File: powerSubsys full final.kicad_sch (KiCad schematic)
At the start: 74 parts, among them J1 Conn_02x16_Odd_Even, J2 JST_PH_2mm, Q2 S9013 J3(RANGE:200-350), SW1 SS-12D11G3R, U1 INA219AIDR, U10 TPS63020DSJR, U2 DRV8833PWR, U3 BQ24074RGT, U4 TPS22810DRVR, U5 TPS22810DRVR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

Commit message: Added power flags
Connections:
- no-connect marks 22 -> 24

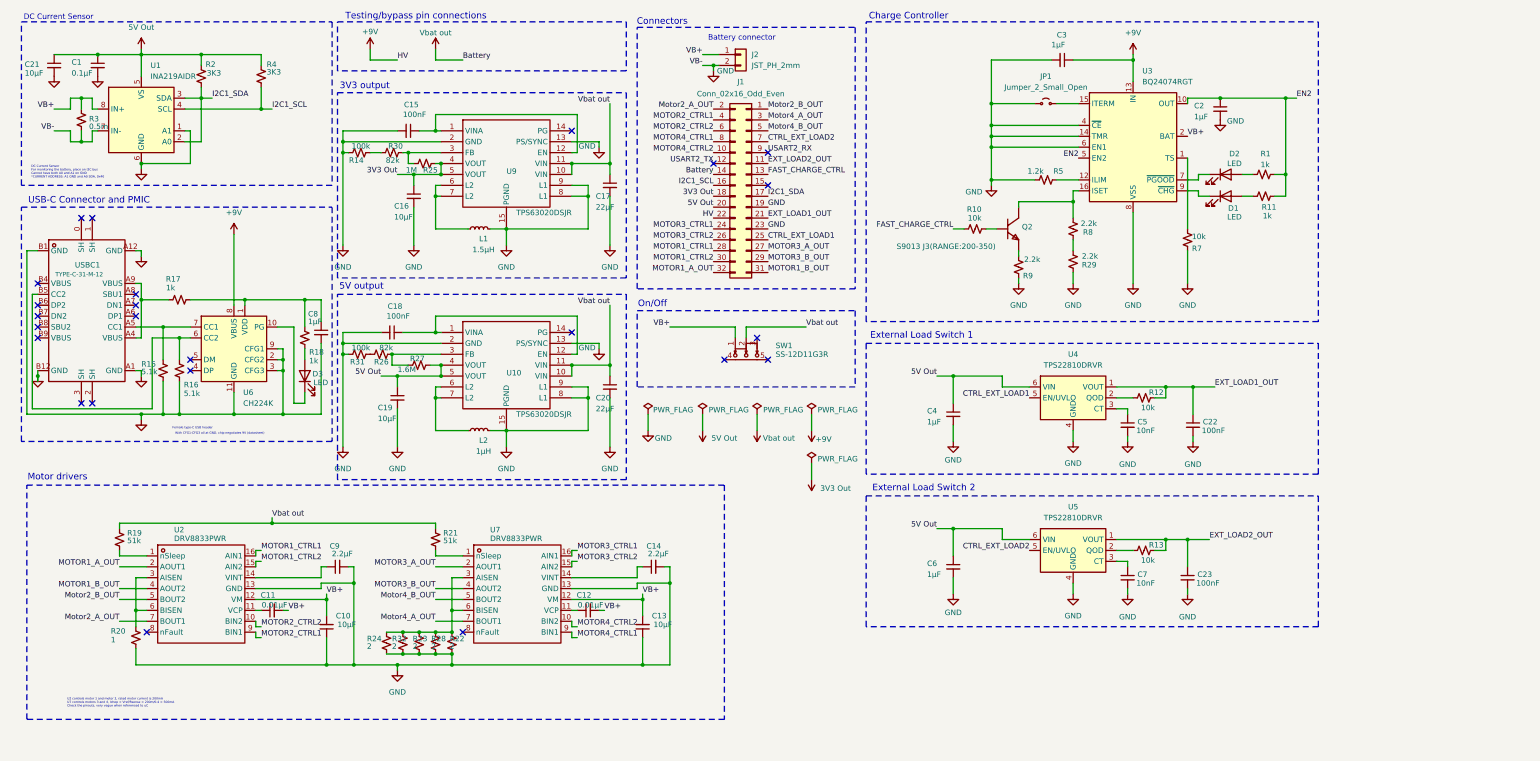
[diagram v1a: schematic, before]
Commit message: Added voltage regulator
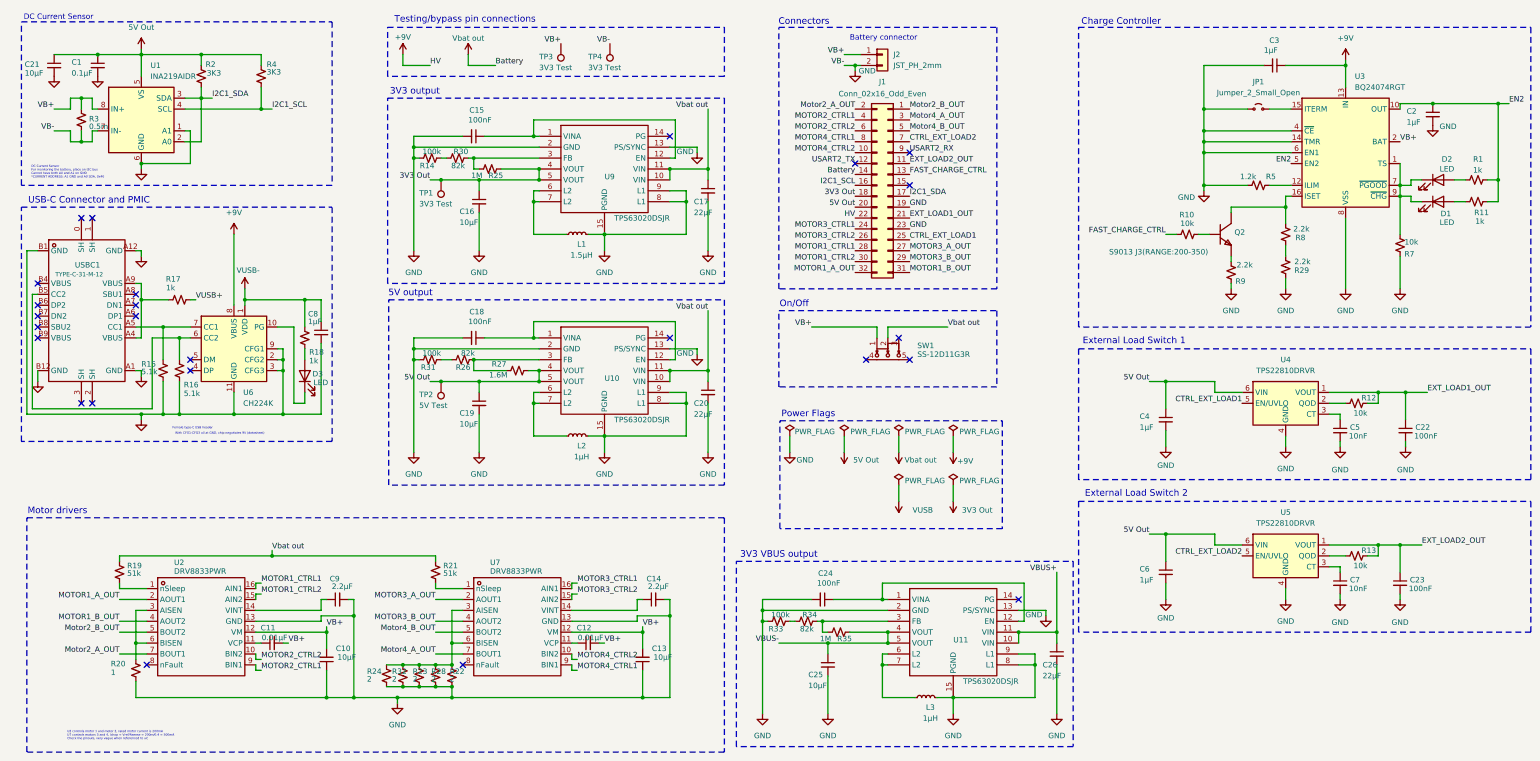
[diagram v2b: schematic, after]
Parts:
- added C24: 100nF, Library:C0603, symbol Device:C_Small
- added C25: 10μF, Library:C0805, symbol Device:C_Small
- added C26: 22μF, Library:C1206, symbol Device:C_Small
- added L3: 1μH, Library:L1008, symbol Device:L_Small
- added R33: 100k, Library:C1206, symbol Device:R_Small_US
- added R34: 82k, Library:C0603, symbol Device:R_Small_US
- added R35: 1M, Library:C1206, symbol Device:R_Small_US
- added TP1, TP3, TP4: 3V3 Test, symbol Connector:TestPoint
- added TP2: 5V Test, symbol Connector:TestPoint
- added U11: TPS63020DSJR, Library:VSON-14_L4.0-W3.0-P0.50-BL-EP_TI_DSJ, symbol TPS63020DSJR1_TPS63020DSJR-altium-import:root_0_TPS63020DSJR_
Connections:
- net 3V3 Out: now also TP1.1
- net 5V Out: now also TP2.1
- net GND: now also C24.2, C25.2, C26.2, L3.2, R33.1, TP4.1, U11.13 (PS/SYNC), U11.15 (PGND), U11.2 (GND), U11.8 (L1), U11.9 (L1)
- net VB+: now also TP3.1
- net VUSB-: now reaches C8.1, R18.1, U6.1 (VDD)
- net VUSB-: no longer R17.2
- net at D2.1 (K), U3.7 (~{PGOOD}): now also D1.1 (K), R7.1, U3.1 (TS), U3.9 (~{CHG})
- new net: R33.2, R34.1
- new net: R34.2, R35.1, U11.3 (FB)
- new net: L3.1, U11.6 (L2), U11.7 (L2)
- new net: C24.1, U11.1 (VINA), U11.12 (EN)
- new net VBUS+: C26.1, U11.10 (VIN), U11.11 (VIN)
- new net VBUS-: C25.1, R35.2, U11.4 (VOUT), U11.5 (VOUT)
- new net VUSB+: R17.2
- no-connect marks 24 -> 25
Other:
- note added: "3V3 VBUS output"
- note added: "Power Flags"
- moved on the sheet: C10, C11, C12, C13, C14, C15, C16, C17, C18, C19, C2, C20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

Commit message: Final
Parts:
- removed L3: 1μH, Library:L1008, symbol Device:L_Small
- removed R17: 1k, Library:C0603, symbol Device:R_Small_US
- removed R34: 82k, Library:C0603, symbol Device:R_Small_US
- removed R35: 1M, Library:C1206, symbol Device:R_Small_US
- removed U11: TPS63020DSJR, Library:VSON-14_L4.0-W3.0-P0.50-BL-EP_TI_DSJ, symbol TPS63020DSJR1_TPS63020DSJR-altium-import:root_0_TPS63020DSJR_
- added TP5: TP +9V, TestPoint:TestPoint_Pad_D1.5mm, symbol Connector:TestPoint
- added TP6: TP VBUS, TestPoint:TestPoint_Pad_D1.5mm, symbol Connector:TestPoint
- added TP7: TS Vsupply, TestPoint:TestPoint_Pad_D1.5mm, symbol Connector:TestPoint
- added TP8: TP VREG, TestPoint:TestPoint_Pad_D1.5mm, symbol Connector:TestPoint
- added U8: L78L33ACUTR, Package_TO_SOT_SMD:SOT-89-3, symbol Regulator_Linear:L78L33_SOT89
- C24: value 100nF -> 1μF; footprint Library:C0603 -> Library:C0805
- C25: value 10μF -> 100nF
- C26: value 22μF -> 10μF; footprint Library:C1206 -> Library:C0805
- D1, D2, D3: value LED -> KT-0805G
- J2: footprint Connector_JST:JST_PH_S2B-PH-SM4-TB_1x02-1MP_P2.00mm_Horizontal -> Connector_JST:JST_PH_S2B-PH-K_1x02_P2.00mm_Horizontal
- JP1: value Jumper_2_Small_Open -> JP RITERM
- R33: value 100k -> 10k; footprint Library:C1206 -> Library:C0603
- TP1: value 3V3 Test -> TP 3V3; footprint (none) -> TestPoint:TestPoint_Pad_D1.5mm
- TP2: value 5V Test -> TP 5V; footprint (none) -> TestPoint:TestPoint_Pad_D1.5mm
- TP3: value 3V3 Test -> TP VBat+; footprint (none) -> TestPoint:TestPoint_Pad_D1.5mm
- TP4: value 3V3 Test -> TP GND; footprint (none) -> TestPoint:TestPoint_Pad_D1.5mm
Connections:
- net VBUS+ is gone; now on net Battery: C26.1
- net VBUS- is gone; now on net GND: C25.1
- net +9V: now also C24.2, R33.1, USBC1.A4 (VBUS), USBC1.A9 (VBUS), TP5.1, TP6.1, U8.3 (IN); no longer U6.8 (VBUS)
- net GND: now also C24.1, U8.2 (GND); no longer C24.2, C25.2, R33.1
- net Motor4_A_OUT: now also R22.1, R23.1, R24.1, R28.1, R32.1, U7.3 (AISEN), U7.6 (BISEN)
- net at R33.2: now also U6.8 (VBUS)
- net DP: now reaches U6.4 (DP)
- net DP: now also USBC1.A6 (DP1)
- net DM: now reaches U6.5 (DM)
- net DM: now also USBC1.A7 (DN1)
- net VB+ renamed Battery
- net Battery: now also J1.14 (Pin_14); no longer C10.2, C11.2, C12.2, C13.2, U2.12 (VM), U7.12 (VM)
- net VUSB- renamed VREG
- net VREG: now also C25.2, TP8.1, U8.1 (OUT)
- net Vbat out renamed Vsupply
- net Vsupply: now also C10.2, C11.2, C12.2, C13.2, U2.12 (VM), U7.12 (VM), TP7.1; no longer J1.14 (Pin_14)
- new net: D2.1 (K), U3.7 (~{PGOOD})
- new net: D1.1 (K), U3.9 (~{CHG})
- new net: R7.1, U3.1 (TS)
- no-connect marks 25 -> 20
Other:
- note added: "3V3 VBUS LDO"
- note removed: "3V3 VBUS output"
- moved on the sheet: C8, D3, R16, R18, R20, R22, R23, R24, R28, R32, TP3

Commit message: Add files via upload
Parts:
- removed JP1: JP RITERM, Library:C1206, symbol Jumper:Jumper_2_Small_Open
- added JP2: SolderJumper_2_Open, Jumper:SolderJumper-2_P1.3mm_Open_RoundedPad1.0x1.5mm, symbol Jumper:SolderJumper_2_Open
- C1: value 0.1μF -> 100nF
- C10, C13, C16, C19, C21, C26: value 10μF -> 10uF
- C11, C12: value 0.01μF -> 10nF
- C14, C9: value 2.2μF -> 2.2uF
- C17, C20: value 22μF -> 22uF
- C2, C24, C3, C4, C6, C8: value 1μF -> 1uF
- C25: footprint Library:C0805 -> Library:C0603
- J1, J2: now not fitted; now left out of the parts list
- L1: value 1.5μH -> 1.5uH
- L2: value 1μH -> 1uH
- Q2: LCSC (none) -> C6749
- R33: footprint Library:C0603 -> Library:C0805
- TP1, TP2, TP3, TP4, TP5, TP6, TP7, TP8: now left out of the parts list
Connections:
- net GND: now also JP2.1 (A)
- net Motor4_A_OUT: no longer R22.1, R23.1, R24.1, R28.1, R32.1, U7.3 (AISEN), U7.6 (BISEN)
- net at U3.15 (ITERM): now also JP2.2 (B)
- new net: R22.1, R23.1, R24.1, R28.1, R32.1, U7.3 (AISEN), U7.6 (BISEN)
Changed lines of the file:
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@@
 	)
 	(junction
-		(at 114.3 162.56)
-		(diameter 0)
-		(color 0 0 0 0)
-	)
-	(junction
 		(at 69.85 35.56)
 		(diameter 0)
@@
 	(wire
 		(pts
-			(xy 114.3 162.56) (xy 114.3 160.02)
-		)
-		(stroke
-			(width 0)
-			(type default)
-		)
-	)
-	(wire
-		(pts
 			(xy 231.14 111.76) (xy 231.14 115.57)
 		)
@@
 	(wire
 		(pts
-			(xy 289.56 35.56) (xy 299.72 35.56)
+			(xy 289.56 35.56) (xy 298.45 35.56)
 		)
 		(stroke
@@
 	(wire
 		(pts
-			(xy 110.49 162.56) (xy 114.3 162.56)
+			(xy 110.49 162.56) (xy 116.84 162.56)
 		)
 		(stroke
@@
 	(wire
 		(pts
-			(xy 304.8 35.56) (xy 309.88 35.56)
+			(xy 322.58 25.4) (xy 322.58 30.48)
 		)
 		(stroke
@@
 	(wire
 		(pts
-			(xy 322.58 25.4) (xy 322.58 30.48)
+			(xy 306.07 35.56) (xy 309.88 35.56)
 		)
 		(stroke
@@
 	(wire
 		(pts
-			(xy 114.3 162.56) (xy 116.84 162.56)
-		)
-		(stroke
-			(width 0)
-			(type default)
-		)
-	)
-	(wire
-		(pts
 			(xy 142.24 154.94) (xy 157.48 154.94)
 		)
@@
 	(wire
 		(pts
-			(xy 114.3 162.56) (xy 114.3 167.64)
+			(xy 114.3 160.02) (xy 114.3 167.64)
 		)
 		(stroke
@@
 			)
 		)
-		(property "Value" "2.2μF"
+		(property "Value" "2.2uF"
 			(at 91.186 146.812 90)
 			(effects
@@
 			)
 		)
-		(property "Value" "10μF"
+		(property "Value" "10uF"
 			(at 91.948 163.322 0)
 			(effects
@@
 			)
 		)
-		(property "Value" "1μH"
+		(property "Value" "1uH"
 			(at 144.526 116.586 90)
 			(effects
@@
 			)
 		)
-		(property "Value" "1μF"
+		(property "Value" "1uF"
 			(at 303.53 21.844 90)
 			(effects
@@
 			)
 		)
-		(property "Footprint" "Library:C0603"
+		(property "Footprint" "Library:C0805"
 			(at 60.96 73.66 0)
 			(effects
@@
 			)
 		)
-		(property "Value" "10μF"
+		(property "Value" "10uF"
 			(at 165.608 163.322 0)
 			(effects
@@
 			)
 		)
-		(property "Value" "1μF"
+		(property "Value" "1uF"
 			(at 336.804 38.608 0)
 			(effects
@@
 		(unit 1)
 		(exclude_from_sim no)
-		(in_bom yes)
+		(in_bom no)
 		(on_board yes)
 		(dnp no)
@@
 			)
 		)
-		(property "Value" "0.01μF"
+		(property "Value" "10nF"
 			(at 75.946 158.75 90)
 			(effects
@@
 			)
 		)
-		(property "Value" "10μF"
+		(property "Value" "10uF"
 			(at 116.078 61.976 0)
 			(effects
@@
 	)
 	(symbol
-		(lib_id "Jumper:Jumper_2_Small_Open")
-		(at 302.26 35.56 0)
-		(unit 1)
-		(exclude_from_sim yes)
-		(in_bom yes)
-		(on_board yes)
-		(dnp no)
-		(fields_autoplaced yes)
-		(property "Reference" "JP1"
-			(at 302.26 29.21 0)
-			(effects
-				(font
-					(size 1.27 1.27)
-				)
-			)
-		)
-		(property "Value" "JP RITERM"
-			(at 302.26 31.75 0)
-			(effects
-				(font
-					(size 1.27 1.27)
-				)
-			)
-		)
-		(property "Footprint" "Library:C1206"
-			(at 302.26 35.56 0)
-			(effects
-				(font
-					(size 1.27 1.27)
-				)
-				(hide yes)
-			)
-		)
-		(property "Datasheet" "~"
-			(at 302.26 35.56 0)
-			(effects
-				(font
-					(size 1.27 1.27)
-				)
-				(hide yes)
-			)
-		)
-		(property "Description" "Jumper, 2-pole, small symbol, open"
-			(at 302.26 35.56 0)
-			(effects
-				(font
-					(size 1.27 1.27)
-				)
-				(hide yes)
-			)
-		)
-		(pin "1"
-		)
-		(pin "2"
-		)
-		(instances
-			(project "powerSubsys full"
-				(path "/7765ff1a-d3b4-4c36-a374-0b467da55076"
-					(reference "JP1")
-					(unit 1)
-				)
-			)
-		)
-	)
-	(symbol
 		(lib_id "power:GND")
 		(at 322.58 77.47 0)
@@
 			)
 		)
-		(property "Value" "1μF"
+		(property "Value" "1uF"
 			(at 210.058 163.322 0)
 			(effects
@@
 			)
 		)
-		(property "Value" "22μF"
+		(property "Value" "22uF"
 			(at 170.688 106.68 0)
 			(effects
@@
 			)
 		)
-		(property "Value" "22μF"
+		(property "Value" "22uF"
 			(at 170.688 59.69 0)
 			(effects
@@
 		(unit 1)
 		(exclude_from_sim no)
-		(in_bom yes)
+		(in_bom no)
 		(on_board yes)
 		(dnp no)
@@
 			)
 		)
-		(property "Value" "0.1μF"
+		(property "Value" "100nF"
 			(at 25.654 27.178 0)
 			(effects
@@
 			)
 		)
-		(property "Value" "0.01μF"
+		(property "Value" "10nF"
 			(at 149.606 158.75 90)
 			(effects
@@
 		(unit 1)
 		(exclude_from_sim no)
-		(in_bom yes)
+		(in_bom no)
 		(on_board yes)
-		(dnp no)
+		(dnp yes)
 		(fields_autoplaced yes)
 		(property "Reference" "J2"
@@
 			)
 		)
-		(property "Value" "1.5μH"
+		(property "Value" "1.5uH"
 			(at 144.526 69.596 90)
 			(effects
@@
 			)
 		)
-		(property "Value" "1μF"
+		(property "Value" "1uF"
 			(at 85.852 85.09 0)
 			(effects
@@
 			)
 		)
-		(property "Footprint" "Library:C0805"
+		(property "Footprint" "Library:C0603"
 			(at 231.14 163.83 0)
 			(effects
@@
 		(unit 1)
 		(exclude_from_sim no)
-		(in_bom yes)
+		(in_bom no)
 		(on_board yes)
 		(dnp no)
@@
 		(unit 1)
 		(exclude_from_sim no)
-		(in_bom yes)
+		(in_bom no)
 		(on_board yes)
-		(dnp no)
+		(dnp yes)
 		(property "Reference" "J1"
 			(at 214.63 29.21 0)
@@
 		(unit 1)
 		(exclude_from_sim no)
-		(in_bom yes)
+		(in_bom no)
 		(on_board yes)
 		(dnp no)
@@
 		(unit 1)
 		(exclude_from_sim no)
-		(in_bom yes)
+		(in_bom no)
 		(on_board yes)
 		(dnp no)
@@
 	)
 	(symbol
+		(lib_id "Jumper:SolderJumper_2_Open")
+		(at 302.26 35.56 0)
+		(unit 1)
+		(exclude_from_sim no)
+		(in_bom no)
+		(on_board yes)
+		(dnp no)
+		(fields_autoplaced yes)
+		(property "Reference" "JP2"
+			(at 302.26 29.21 0)
+			(effects
+				(font
+					(size 1.27 1.27)
+				)
+			)
+		)
+		(property "Value" "SolderJumper_2_Open"
+			(at 302.26 31.75 0)
+			(effects
+				(font
+					(size 1.27 1.27)
+				)
+			)
+		)
+		(property "Footprint" "Jumper:SolderJumper-2_P1.3mm_Open_RoundedPad1.0x1.5mm"
+			(at 302.26 35.56 0)
+			(effects
+				(font
+					(size 1.27 1.27)
+				)
+				(hide yes)
+			)
+		)
+		(property "Datasheet" "~"
+			(at 302.26 35.56 0)
+			(effects
+				(font
+					(size 1.27 1.27)
+				)
+				(hide yes)
+			)
+		)
+		(property "Description" "Solder Jumper, 2-pole, open"
+			(at 302.26 35.56 0)
+			(effects
+				(font
+					(size 1.27 1.27)
+				)
+				(hide yes)
+			)
+		)
+		(pin "2"
+		)
+		(pin "1"
+		)
+		(instances
+			(project ""
+				(path "/7765ff1a-d3b4-4c36-a374-0b467da55076"
+					(reference "JP2")
+					(unit 1)
+				)
+			)
+		)
+	)
+	(symbol
 		(lib_id "Device:C_Small")
 		(at 280.67 107.95 0)
@@
 			)
 		)
-		(property "Value" "1μF"
+		(property "Value" "1uF"
 			(at 274.574 109.728 0)
 			(effects
@@
 			)
 		)
-		(property "Value" "10μF"
+		(property "Value" "10uF"
 			(at 116.078 108.966 0)
 			(effects
@@
 			)
 		)
-		(property "Value" "1μF"
+		(property "Value" "1uF"
 			(at 274.574 145.288 0)
 			(effects
@@
 			)
 		)
-		(property "Value" "10μF"
+		(property "Value" "10uF"
 			(at 335.534 47.498 0)
 			(effects
@@
 		(unit 1)
 		(exclude_from_sim no)
-		(in_bom yes)
+		(in_bom no)
 		(on_board yes)
 		(dnp no)
@@
 			)
 		)
+		(property "LCSC" "C6749"
+			(at 293.37 64.77 0)
+			(effects
+				(font
+					(size 1.27 1.27)
+				)
+				(hide yes)
+			)
+		)
 		(pin "2"
 		)
@@
 		(unit 1)
 		(exclude_from_sim no)
-		(in_bom yes)
+		(in_bom no)
 		(on_board yes)
 		(dnp no)
@@
 			)
 		)
-		(property "Value" "2.2μF"
+		(property "Value" "2.2uF"
 			(at 164.846 146.812 90)
 			(effects
@@
 		(unit 1)
 		(exclude_from_sim no)
-		(in_bom yes)
+		(in_bom no)
 		(on_board yes)
 		(dnp no)
@@
 			)
 		)
-		(property "Value" "10μF"
+		(property "Value" "10uF"
 			(at 14.732 27.178 0)
 			(effects
